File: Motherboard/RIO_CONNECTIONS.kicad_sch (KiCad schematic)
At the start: 18 parts, among them U1A LM358, U1B LM358, U2A LM358, U2B LM358

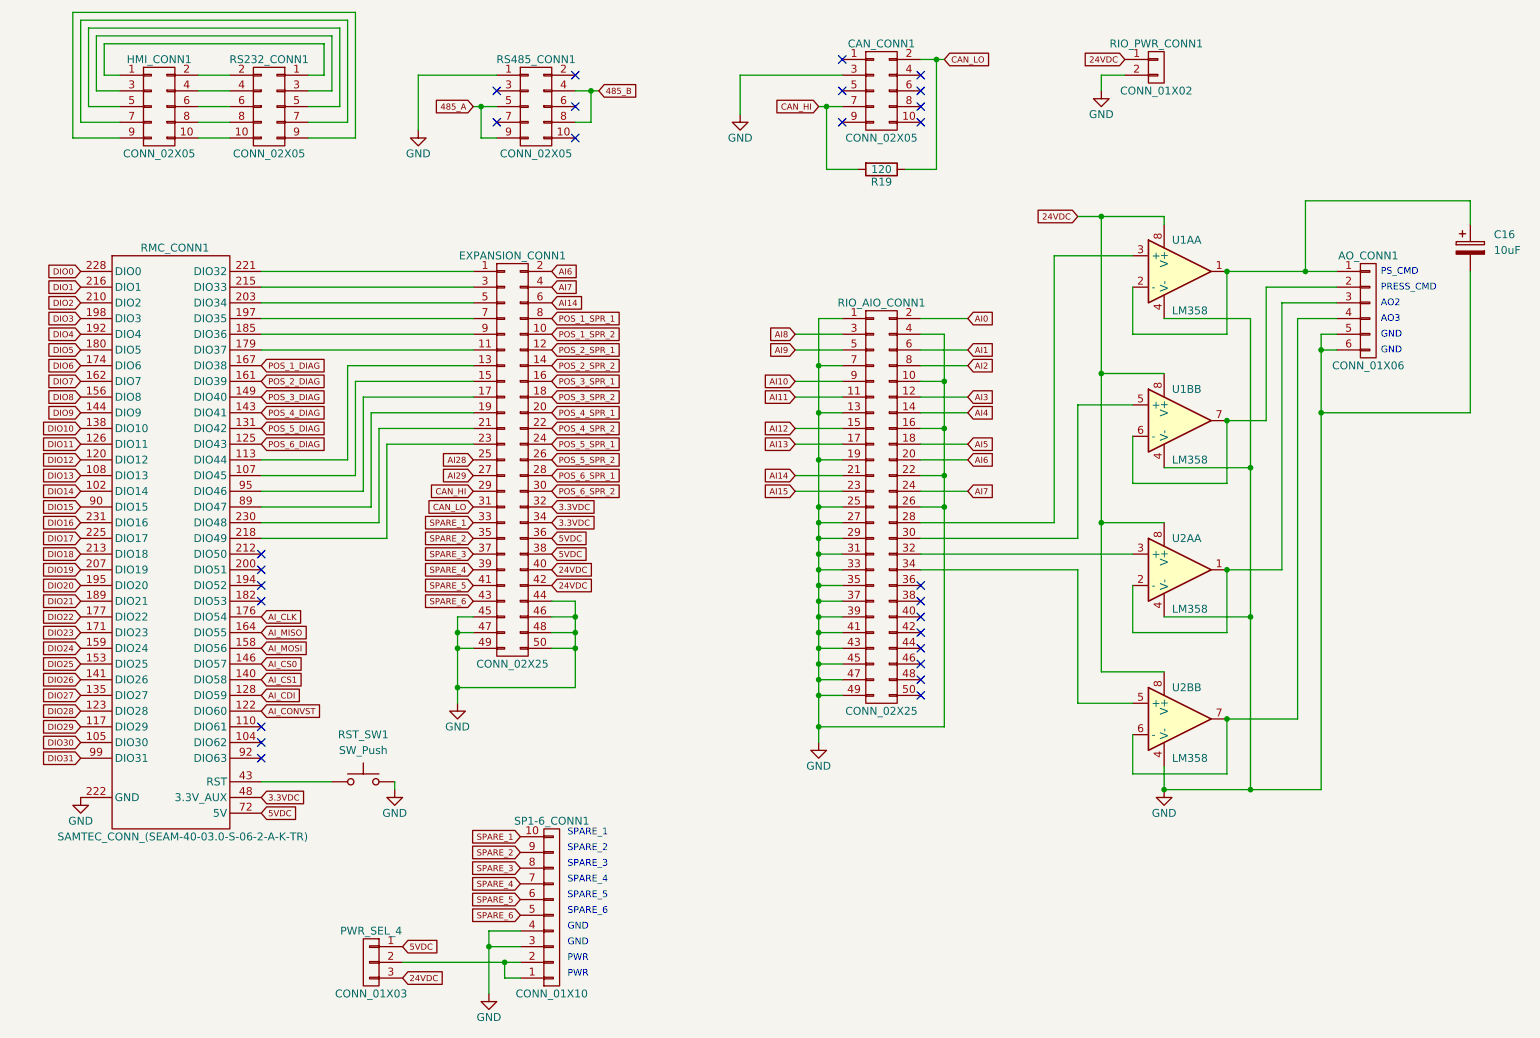
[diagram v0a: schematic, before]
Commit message: Schematic ready.  Going to clean up directory now.
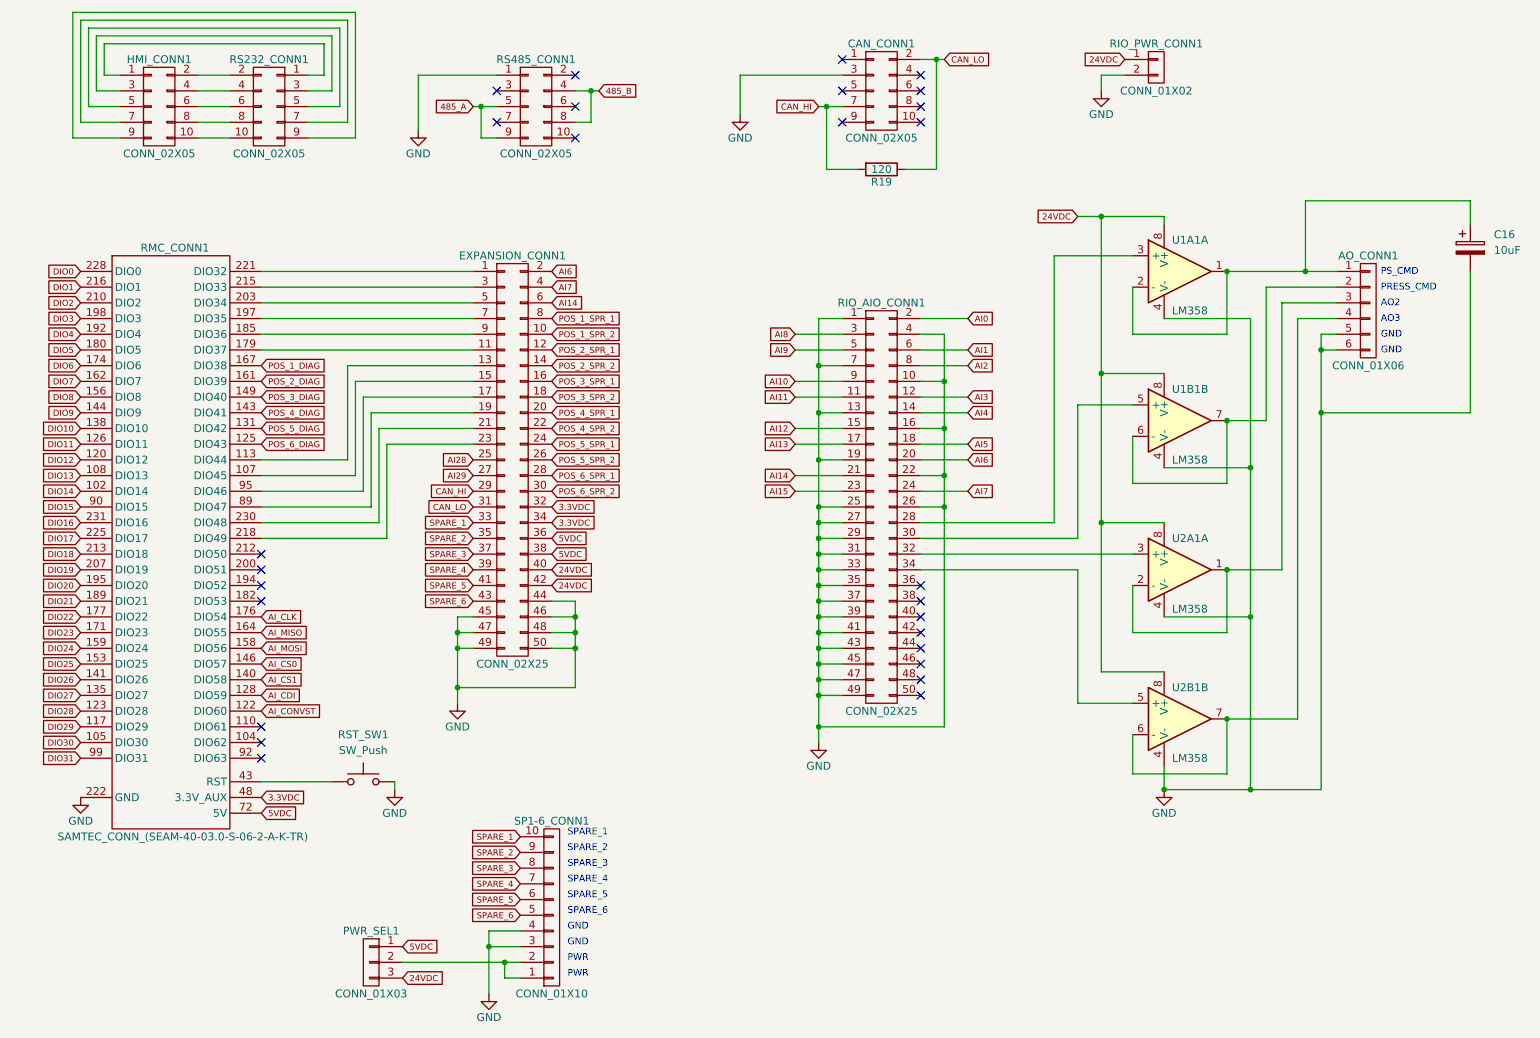
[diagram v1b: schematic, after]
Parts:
- C16: footprint (none) -> Smart_Tank:CAP_EEEHD1C100AR
- CAN_CONN1, HMI_CONN1, RS232_CONN1, RS485_CONN1: footprint Connect:IDC_Header_Straight_10pins -> Connector_IDC:IDC-Header_2x05_P2.54mm_Vertical
- EXPANSION_CONN1: footprint Connect:IDC_Header_Straight_50pins -> Connector_IDC:IDC-Header_2x25_P2.54mm_Vertical
- PWR_SEL1: renamed from PWR_SEL_4; footprint Pin_Headers:Pin_Header_Straight_1x03_Pitch2.54mm -> Connector_PinHeader_2.54mm:PinHeader_1x03_P2.54mm_Vertical
- R19: footprint Resistors_SMD:R_1206 -> Resistor_SMD:R_1206_3216Metric
- RIO_PWR_CONN1: footprint Smart_Tank:MOLEX_2-PIN_CONN_(0039300020) -> Smart_Tank:PHNX_TB_SCREW_2_POS_(1729128)
- RST_SW1: footprint (none) -> Button_Switch_SMD:SW_SPST_Omron_B3FS-100xP
- U1A1: renamed from U1A; footprint Housings_SOIC:SOIC-8_3.9x4.9mm_Pitch1.27mm -> Package_SO:SOIC-8_3.9x4.9mm_P1.27mm
- U1B1: renamed from U1B; footprint Housings_SOIC:SOIC-8_3.9x4.9mm_Pitch1.27mm -> Package_SO:SOIC-8_3.9x4.9mm_P1.27mm
- U2A1: renamed from U2A; footprint Housings_SOIC:SOIC-8_3.9x4.9mm_Pitch1.27mm -> Package_SO:SOIC-8_3.9x4.9mm_P1.27mm
- U2B1: renamed from U2B; footprint Housings_SOIC:SOIC-8_3.9x4.9mm_Pitch1.27mm -> Package_SO:SOIC-8_3.9x4.9mm_P1.27mm
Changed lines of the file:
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@@
 			)
 		)
-		(property "Footprint" "Connect:IDC_Header_Straight_50pins"
+		(property "Footprint" "Connector_IDC:IDC-Header_2x25_P2.54mm_Vertical"
 			(at 106.68 116.84 0)
 			(effects
@@
 			)
 		)
-		(property "Footprint" "Connect:IDC_Header_Straight_10pins"
+		(property "Footprint" "Connector_IDC:IDC-Header_2x05_P2.54mm_Vertical"
 			(at 166.37 68.58 0)
 			(effects
@@
 			)
 		)
-		(property "Footprint" "Smart_Tank:MOLEX_2-PIN_CONN_(0039300020)"
+		(property "Footprint" "Smart_Tank:PHNX_TB_SCREW_2_POS_(1729128)"
 			(at 210.82 34.29 0)
 			(effects
@@
 		(on_board yes)
 		(dnp no)
-		(property "Reference" "U1A"
+		(property "Reference" "U1A1"
 			(at 213.36 62.23 0)
 			(effects
@@
 			)
 		)
-		(property "Footprint" "Housings_SOIC:SOIC-8_3.9x4.9mm_Pitch1.27mm"
+		(property "Footprint" "Package_SO:SOIC-8_3.9x4.9mm_P1.27mm"
 			(at 214.63 67.31 0)
 			(effects
@@
 			(project "Smart Tank Motherboard"
 				(path "/9bd0ace5-d8c1-442c-86d3-58cb44e43f85/00000000-0000-0000-0000-0000578fba35"
-					(reference "U1A")
+					(reference "U1A1")
 					(unit 1)
 				)
@@
 		(on_board yes)
 		(dnp no)
-		(property "Reference" "U1B"
+		(property "Reference" "U1B1"
 			(at 213.36 86.36 0)
 			(effects
@@
 			)
 		)
-		(property "Footprint" "Housings_SOIC:SOIC-8_3.9x4.9mm_Pitch1.27mm"
+		(property "Footprint" "Package_SO:SOIC-8_3.9x4.9mm_P1.27mm"
 			(at 214.63 91.44 0)
 			(effects
@@
 			(project "Smart Tank Motherboard"
 				(path "/9bd0ace5-d8c1-442c-86d3-58cb44e43f85/00000000-0000-0000-0000-0000578fba35"
-					(reference "U1B")
+					(reference "U1B1")
 					(unit 2)
 				)
@@
 		(on_board yes)
 		(dnp no)
-		(property "Reference" "U2A"
+		(property "Reference" "U2A1"
 			(at 213.36 110.49 0)
 			(effects
@@
 			)
 		)
-		(property "Footprint" "Housings_SOIC:SOIC-8_3.9x4.9mm_Pitch1.27mm"
+		(property "Footprint" "Package_SO:SOIC-8_3.9x4.9mm_P1.27mm"
 			(at 214.63 115.57 0)
 			(effects
@@
 			(project "Smart Tank Motherboard"
 				(path "/9bd0ace5-d8c1-442c-86d3-58cb44e43f85/00000000-0000-0000-0000-0000578fba35"
-					(reference "U2A")
+					(reference "U2A1")
 					(unit 1)
 				)
@@
 			)
 		)
-		(property "Footprint" "Resistors_SMD:R_1206"
+		(property "Footprint" "Resistor_SMD:R_1206_3216Metric"
 			(at 166.37 49.022 90)
 			(effects
@@
 		(on_board yes)
 		(dnp no)
-		(property "Reference" "U2B"
+		(property "Reference" "U2B1"
 			(at 213.36 134.62 0)
 			(effects
@@
 			)
 		)
-		(property "Footprint" "Housings_SOIC:SOIC-8_3.9x4.9mm_Pitch1.27mm"
+		(property "Footprint" "Package_SO:SOIC-8_3.9x4.9mm_P1.27mm"
 			(at 214.63 139.7 0)
 			(effects
@@
 			(project "Smart Tank Motherboard"
 				(path "/9bd0ace5-d8c1-442c-86d3-58cb44e43f85/00000000-0000-0000-0000-0000578fba35"
-					(reference "U2B")
+					(reference "U2B1")
 					(unit 2)
 				)
@@
 		(on_board yes)
 		(dnp no)
-		(property "Reference" "PWR_SEL_4"
+		(property "Reference" "PWR_SEL1"
 			(at 83.82 173.99 0)
 			(effects
@@
 			)
 		)
-		(property "Footprint" "Pin_Headers:Pin_Header_Straight_1x03_Pitch2.54mm"
+		(property "Footprint" "Connector_PinHeader_2.54mm:PinHeader_1x03_P2.54mm_Vertical"
 			(at 83.82 179.07 0)
 			(effects
@@
 			(project "Smart Tank Motherboard"
 				(path "/9bd0ace5-d8c1-442c-86d3-58cb44e43f85/00000000-0000-0000-0000-0000578fba35"
-					(reference "PWR_SEL_4")
+					(reference "PWR_SEL1")
 					(unit 1)
 				)
@@
 			)
 		)
-		(property "Footprint" "Connect:IDC_Header_Straight_10pins"
+		(property "Footprint" "Connector_IDC:IDC-Header_2x05_P2.54mm_Vertical"
 			(at 49.53 71.12 0)
 			(effects
@@
 			)
 		)
-		(property "Footprint" "Connect:IDC_Header_Straight_10pins"
+		(property "Footprint" "Connector_IDC:IDC-Header_2x05_P2.54mm_Vertical"
 			(at 110.49 71.12 0)
 			(effects
@@
 			)
 		)
-		(property "Footprint" ""
+		(property "Footprint" "Button_Switch_SMD:SW_SPST_Omron_B3FS-100xP"
 			(at 82.55 144.78 0)
 			(effects
@@
 			)
 		)
-		(property "Footprint" "Connect:IDC_Header_Straight_10pins"
+		(property "Footprint" "Connector_IDC:IDC-Header_2x05_P2.54mm_Vertical"
 			(at 67.31 71.12 0)
 			(effects
@@
 			)
 		)
-		(property "Footprint" ""
+		(property "Footprint" "Smart_Tank:CAP_EEEHD1C100AR"
 			(at 262.5852 67.31 0)
 			(effects

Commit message: Started cleaning out old parts from PCB.
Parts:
- renumbered U1A1 to U1, U1B1 to U1, U2A1 to U2, U2B1 to U2
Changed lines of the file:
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@@
 		(on_board yes)
 		(dnp no)
-		(property "Reference" "U1A1"
+		(property "Reference" "U1"
 			(at 213.36 62.23 0)
 			(effects
@@
 			(project "Smart Tank Motherboard"
 				(path "/9bd0ace5-d8c1-442c-86d3-58cb44e43f85/00000000-0000-0000-0000-0000578fba35"
-					(reference "U1A1")
+					(reference "U1")
 					(unit 1)
 				)
@@
 		(on_board yes)
 		(dnp no)
-		(property "Reference" "U1B1"
+		(property "Reference" "U1"
 			(at 213.36 86.36 0)
 			(effects
@@
 			(project "Smart Tank Motherboard"
 				(path "/9bd0ace5-d8c1-442c-86d3-58cb44e43f85/00000000-0000-0000-0000-0000578fba35"
-					(reference "U1B1")
+					(reference "U1")
 					(unit 2)
 				)
@@
 		(on_board yes)
 		(dnp no)
-		(property "Reference" "U2A1"
+		(property "Reference" "U2"
 			(at 213.36 110.49 0)
 			(effects
@@
 			(project "Smart Tank Motherboard"
 				(path "/9bd0ace5-d8c1-442c-86d3-58cb44e43f85/00000000-0000-0000-0000-0000578fba35"
-					(reference "U2A1")
+					(reference "U2")
 					(unit 1)
 				)
@@
 		(on_board yes)
 		(dnp no)
-		(property "Reference" "U2B1"
+		(property "Reference" "U2"
 			(at 213.36 134.62 0)
 			(effects
@@
 			(project "Smart Tank Motherboard"
 				(path "/9bd0ace5-d8c1-442c-86d3-58cb44e43f85/00000000-0000-0000-0000-0000578fba35"
-					(reference "U2B1")
+					(reference "U2")
 					(unit 2)
 				)

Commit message: Continued cleanup and reconnects.
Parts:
- CAN_CONN1, HMI_CONN1, RS232_CONN1, RS485_CONN1: footprint Connector_IDC:IDC-Header_2x05_P2.54mm_Vertical -> Connect:IDC_Header_Straight_10pins
- EXPANSION_CONN1: footprint Connector_IDC:IDC-Header_2x25_P2.54mm_Vertical -> Connect:IDC_Header_Straight_50pins
- U1, U2: footprint Package_SO:SOIC-8_3.9x4.9mm_P1.27mm -> Housings_SOIC:SOIC-8_3.9x4.9mm_Pitch1.27mm
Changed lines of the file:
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@@
 			)
 		)
-		(property "Footprint" "Connector_IDC:IDC-Header_2x25_P2.54mm_Vertical"
+		(property "Footprint" "Connect:IDC_Header_Straight_50pins"
 			(at 106.68 116.84 0)
 			(effects
@@
 			)
 		)
-		(property "Footprint" "Connector_IDC:IDC-Header_2x05_P2.54mm_Vertical"
+		(property "Footprint" "Connect:IDC_Header_Straight_10pins"
 			(at 166.37 68.58 0)
 			(effects
@@
 			)
 		)
-		(property "Footprint" "Package_SO:SOIC-8_3.9x4.9mm_P1.27mm"
+		(property "Footprint" "Housings_SOIC:SOIC-8_3.9x4.9mm_Pitch1.27mm"
 			(at 214.63 67.31 0)
 			(effects
@@
 			)
 		)
-		(property "Footprint" "Package_SO:SOIC-8_3.9x4.9mm_P1.27mm"
+		(property "Footprint" "Housings_SOIC:SOIC-8_3.9x4.9mm_Pitch1.27mm"
 			(at 214.63 91.44 0)
 			(effects
@@
 			)
 		)
-		(property "Footprint" "Package_SO:SOIC-8_3.9x4.9mm_P1.27mm"
+		(property "Footprint" "Housings_SOIC:SOIC-8_3.9x4.9mm_Pitch1.27mm"
 			(at 214.63 115.57 0)
 			(effects
@@
 			)
 		)
-		(property "Footprint" "Package_SO:SOIC-8_3.9x4.9mm_P1.27mm"
+		(property "Footprint" "Housings_SOIC:SOIC-8_3.9x4.9mm_Pitch1.27mm"
 			(at 214.63 139.7 0)
 			(effects
@@
 			)
 		)
-		(property "Footprint" "Connector_IDC:IDC-Header_2x05_P2.54mm_Vertical"
+		(property "Footprint" "Connect:IDC_Header_Straight_10pins"
 			(at 49.53 71.12 0)
 			(effects
@@
 			)
 		)
-		(property "Footprint" "Connector_IDC:IDC-Header_2x05_P2.54mm_Vertical"
+		(property "Footprint" "Connect:IDC_Header_Straight_10pins"
 			(at 110.49 71.12 0)
 			(effects
@@
 			)
 		)
-		(property "Footprint" "Connector_IDC:IDC-Header_2x05_P2.54mm_Vertical"
+		(property "Footprint" "Connect:IDC_Header_Straight_10pins"
 			(at 67.31 71.12 0)
 			(effects
